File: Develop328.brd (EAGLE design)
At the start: 100 x 80 mm, 0 parts

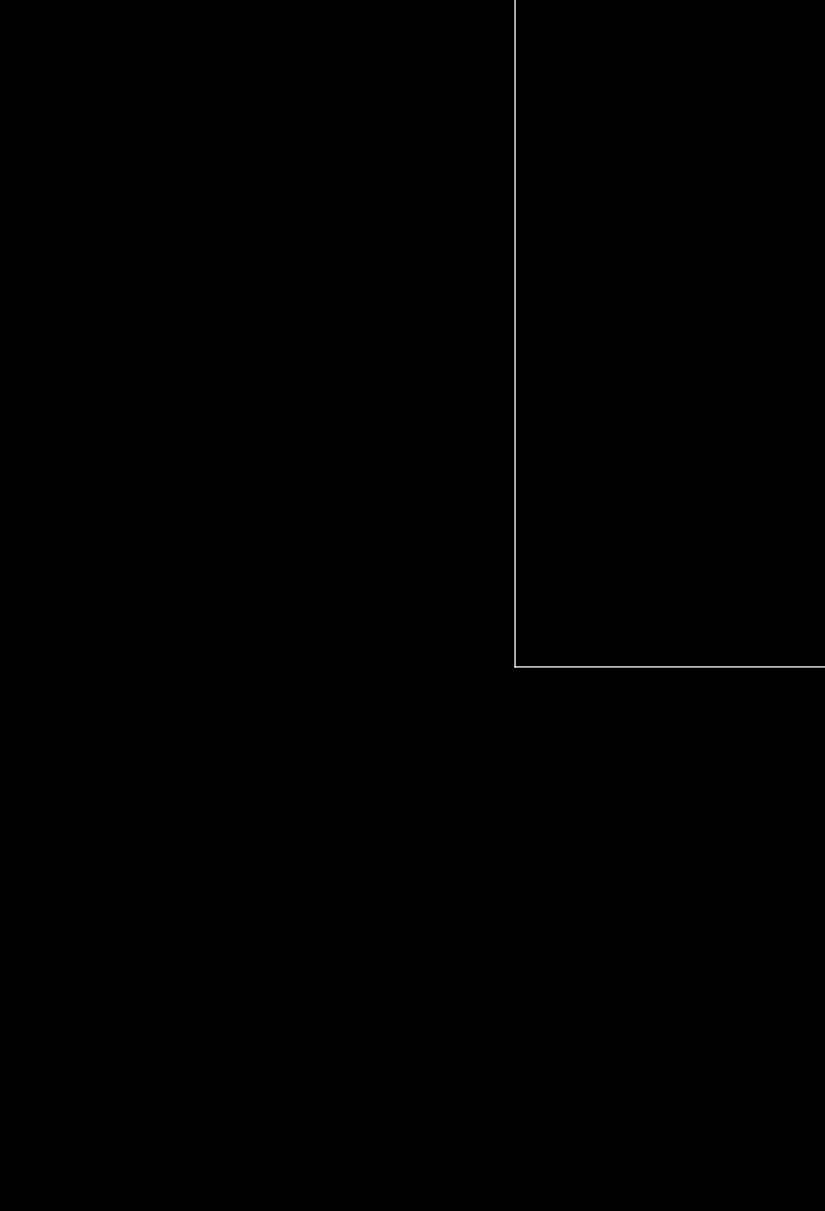
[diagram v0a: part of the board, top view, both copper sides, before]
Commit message: Added first round of components to schematic
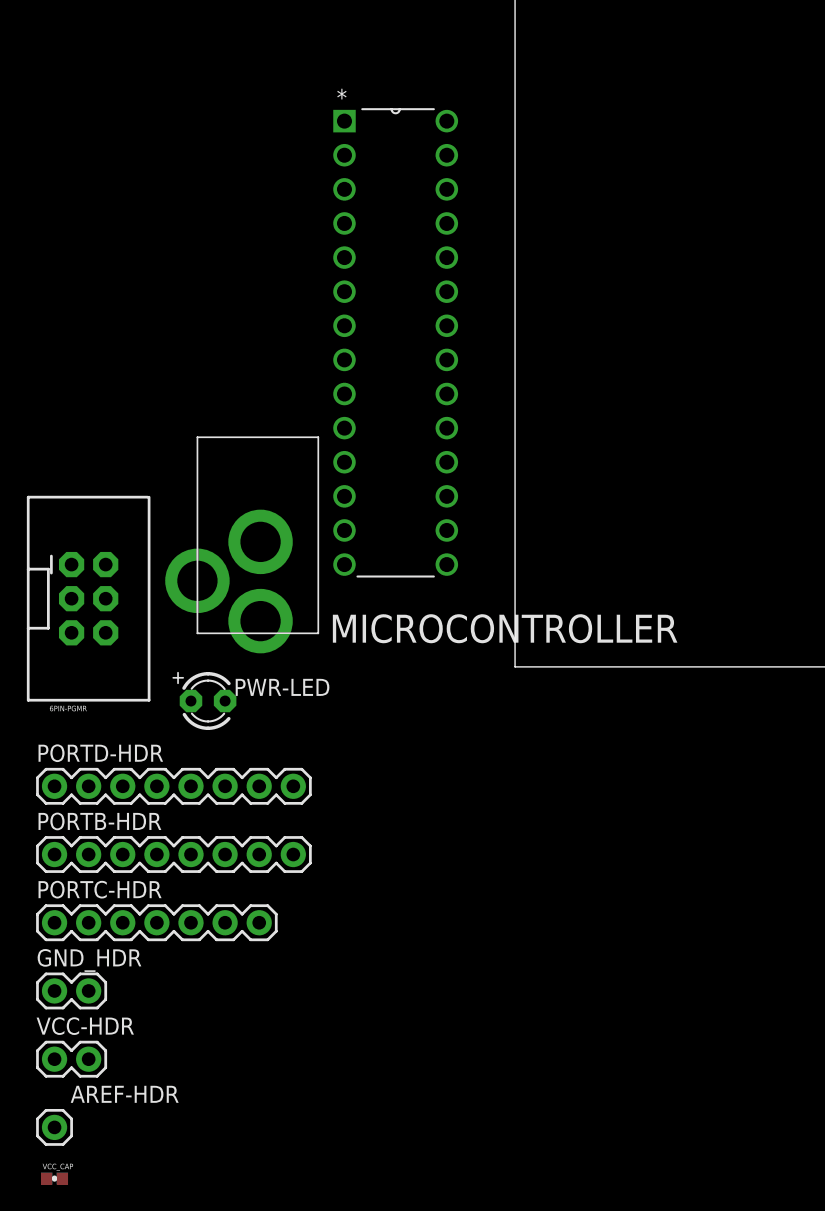
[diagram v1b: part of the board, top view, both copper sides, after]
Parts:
- added 5V-DC-JACK: (no value), adafruit:PJ-102A
- added 6PIN-PGMR: (no value), SparkFun-Connectors:2X3-SHROUDED
- added AREF-HDR: (no value), SparkFun-Connectors:1X01
- added GND_HDR, VCC-HDR: (no value), SparkFun-Connectors:1X02
- added MICROCONTROLLER: ATMEGA328P-PU, Atmel_By_element14_Batch_1-00:DIP254P762X457-28
- added PORTB-HDR, PORTD-HDR: (no value), SparkFun-Connectors:1X08_ROUND
- added PORTC-HDR: (no value), SparkFun-Connectors:1X07
- added PWR-LED: (no value), adafruit:LED3MM
- added VCC_CAP: 0.1uF, SparkFun-Capacitors:0402-CAP
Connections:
- new net AVCC: MICROCONTROLLER.20
- new net VCC: MICROCONTROLLER.7

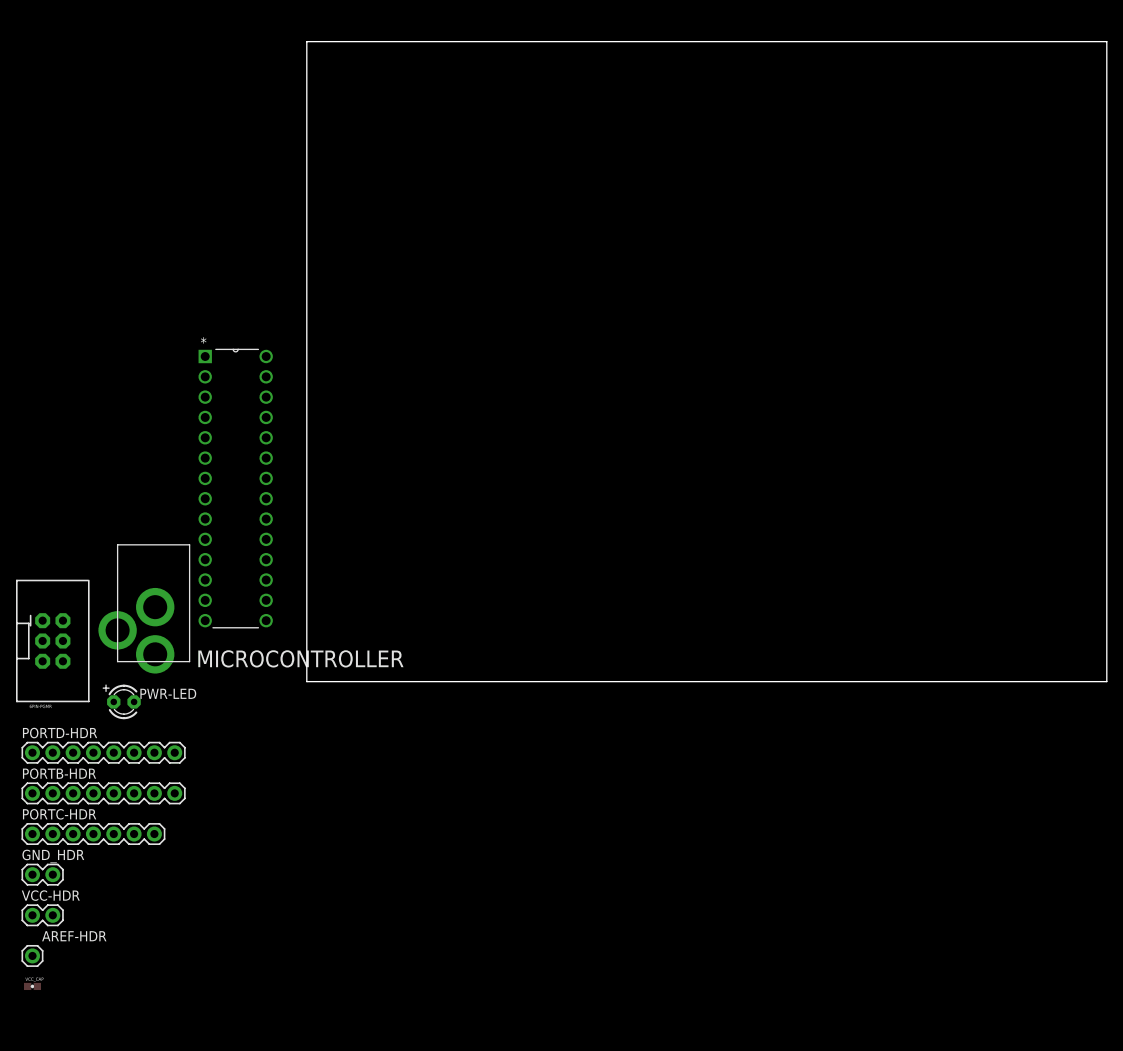
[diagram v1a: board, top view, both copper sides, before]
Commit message: Added wires to all port headers
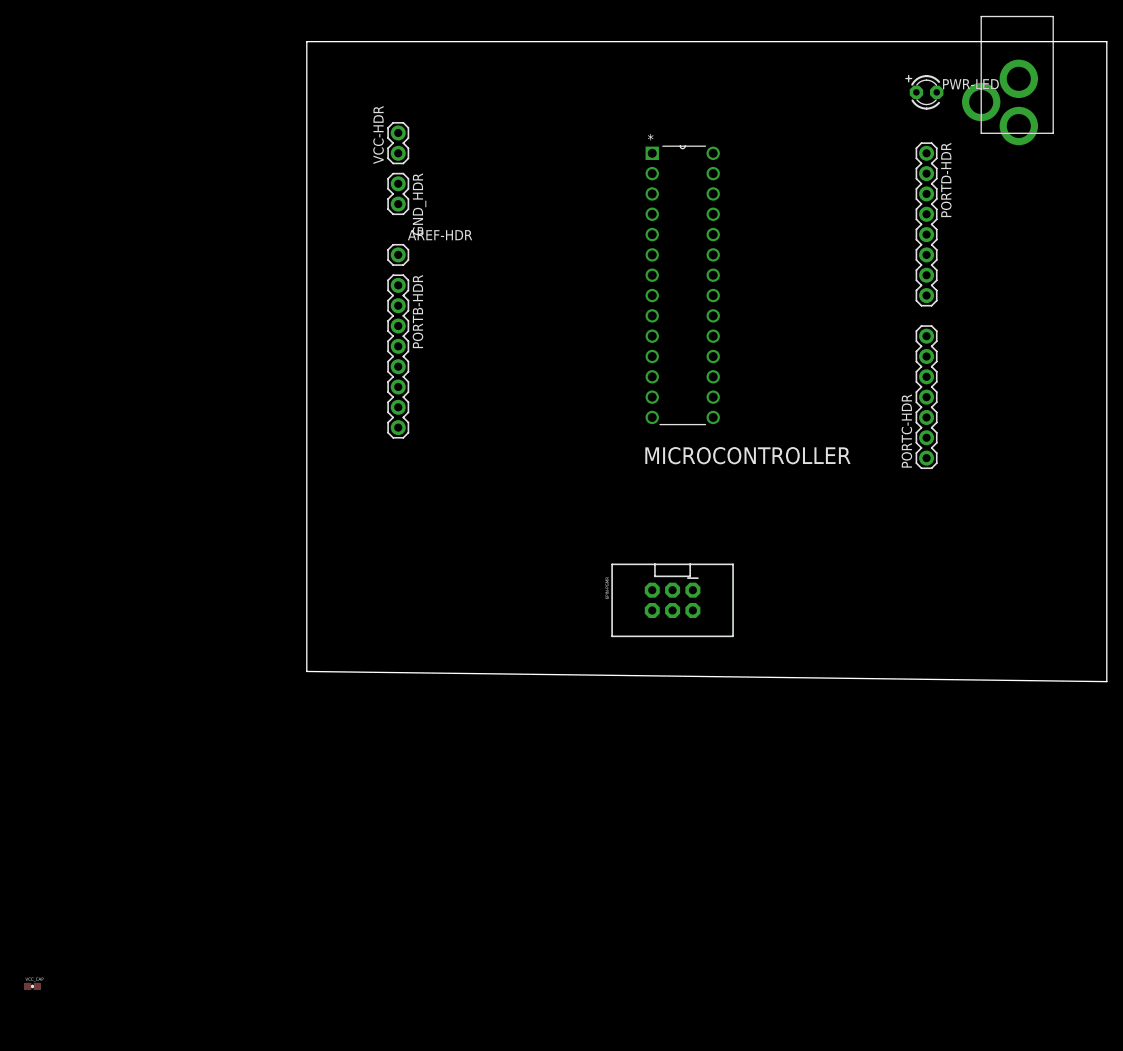
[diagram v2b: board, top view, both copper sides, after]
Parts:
- moved PORTD-HDR 134.6 mm to (77.5, 66.0), turned to 270 degrees
- moved 5V-DC-JACK 126.5 mm to (88.9, 78.7)
- moved PWR-LED 126.0 mm to (77.5, 73.7)
- moved PORTC-HDR 121.2 mm to (77.5, 27.9), turned to 90 degrees
- moved VCC-HDR 105.7 mm to (11.4, 66.0), turned to 90 degrees
- moved AREF-HDR 98.8 mm to (11.4, 53.3)
- moved GND_HDR 97.7 mm to (11.4, 62.2), turned to 270 degrees
- moved PORTB-HDR 78.2 mm to (11.4, 49.5), turned to 270 degrees
- moved 6PIN-PGMR 77.6 mm to (45.7, 10.2), turned to 270 degrees
- moved MICROCONTROLLER 61.4 mm to (50.8, 33.0)
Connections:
- removed net AVCC: MICROCONTROLLER.20
- removed net VCC: MICROCONTROLLER.7
- new net N$1: MICROCONTROLLER.7, VCC-HDR.2
- new net N$10: MICROCONTROLLER.13, PORTD-HDR.8
- new net N$11: MICROCONTROLLER.23, PORTC-HDR.1
- new net N$12: MICROCONTROLLER.24, PORTC-HDR.2
- new net N$13: MICROCONTROLLER.25, PORTC-HDR.3
- new net N$14: MICROCONTROLLER.26, PORTC-HDR.4
- new net N$15: MICROCONTROLLER.27, PORTC-HDR.5
- new net N$16: MICROCONTROLLER.28, PORTC-HDR.6
- new net N$17: MICROCONTROLLER.1, PORTC-HDR.7
- new net N$18: MICROCONTROLLER.14, PORTB-HDR.8
- new net N$19: MICROCONTROLLER.15, PORTB-HDR.7
- new net N$2: GND_HDR.1, MICROCONTROLLER.22
- new net N$20: MICROCONTROLLER.16, PORTB-HDR.6
- new net N$21: MICROCONTROLLER.17, PORTB-HDR.5
- new net N$22: MICROCONTROLLER.18, PORTB-HDR.4
- new net N$23: MICROCONTROLLER.19, PORTB-HDR.3
- new net N$24: MICROCONTROLLER.9, PORTB-HDR.2
- new net N$25: MICROCONTROLLER.10, PORTB-HDR.1
- new net N$26: AREF-HDR.1, MICROCONTROLLER.21
- new net N$27: MICROCONTROLLER.20, VCC-HDR.1
- new net N$28: GND_HDR.2, MICROCONTROLLER.8
- new net N$3: MICROCONTROLLER.2, PORTD-HDR.1
- new net N$4: MICROCONTROLLER.3, PORTD-HDR.2
- new net N$5: MICROCONTROLLER.4, PORTD-HDR.3
- new net N$6: MICROCONTROLLER.5, PORTD-HDR.4
- new net N$7: MICROCONTROLLER.6, PORTD-HDR.5
- new net N$8: MICROCONTROLLER.11, PORTD-HDR.6
- new net N$9: MICROCONTROLLER.12, PORTD-HDR.7
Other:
- outline, holes or cut-outs redrawn

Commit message: Replaced wires with electrical connections
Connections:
- removed net N$1 (its old number): MICROCONTROLLER.7, VCC-HDR.2
- removed net N$2 (its old number): GND_HDR.1, MICROCONTROLLER.22
- removed net N$27: MICROCONTROLLER.20, VCC-HDR.1
- removed net N$28: GND_HDR.2, MICROCONTROLLER.8
- new net AVCC: MICROCONTROLLER.20
- new net VCC: MICROCONTROLLER.7
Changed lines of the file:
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@@
 </elements>
 <signals>
-<signal name="N$2">
-<contactref element="MICROCONTROLLER" pad="22"/>
-<contactref element="GND_HDR" pad="1"/>
-<wire x1="11.43" y1="62.23" x2="50.8" y2="50.8" width="0" layer="19" extent="1-1"/>
+<signal name="VCC">
+<contactref element="MICROCONTROLLER" pad="7"/>
 </signal>
-<signal name="N$18">
+<signal name="AVCC">
+<contactref element="MICROCONTROLLER" pad="20"/>
+</signal>
+<signal name="N$1">
 <contactref element="PORTB-HDR" pad="8"/>
 <contactref element="MICROCONTROLLER" pad="14"/>
-<wire x1="43.18" y1="33.02" x2="11.43" y2="31.75" width="0" layer="19" extent="1-1"/>
+<wire x1="11.43" y1="31.75" x2="43.18" y2="33.02" width="0" layer="19" extent="1-1"/>
 </signal>
-<signal name="N$19">
+<signal name="N$2">
 <contactref element="PORTB-HDR" pad="7"/>
 <contactref element="MICROCONTROLLER" pad="15"/>
-<wire x1="50.8" y1="33.02" x2="11.43" y2="34.29" width="0" layer="19" extent="1-1"/>
+<wire x1="11.43" y1="34.29" x2="50.8" y2="33.02" width="0" layer="19" extent="1-1"/>
 </signal>
-<signal name="N$20">
+<signal name="N$3">
 <contactref element="PORTB-HDR" pad="6"/>
 <contactref element="MICROCONTROLLER" pad="16"/>
-<wire x1="50.8" y1="35.56" x2="11.43" y2="36.83" width="0" layer="19" extent="1-1"/>
+<wire x1="11.43" y1="36.83" x2="50.8" y2="35.56" width="0" layer="19" extent="1-1"/>
 </signal>
-<signal name="N$21">
+<signal name="N$4">
 <contactref element="PORTB-HDR" pad="5"/>
 <contactref element="MICROCONTROLLER" pad="17"/>
-<wire x1="50.8" y1="38.1" x2="11.43" y2="39.37" width="0" layer="19" extent="1-1"/>
+<wire x1="11.43" y1="39.37" x2="50.8" y2="38.1" width="0" layer="19" extent="1-1"/>
 </signal>
-<signal name="N$22">
+<signal name="N$5">
 <contactref element="PORTB-HDR" pad="4"/>
 <contactref element="MICROCONTROLLER" pad="18"/>
-<wire x1="50.8" y1="40.64" x2="11.43" y2="41.91" width="0" layer="19" extent="1-1"/>
+<wire x1="11.43" y1="41.91" x2="50.8" y2="40.64" width="0" layer="19" extent="1-1"/>
 </signal>
-<signal name="N$23">
+<signal name="N$6">
 <contactref element="PORTB-HDR" pad="3"/>
 <contactref element="MICROCONTROLLER" pad="19"/>
-<wire x1="50.8" y1="43.18" x2="11.43" y2="44.45" width="0" layer="19" extent="1-1"/>
+<wire x1="11.43" y1="44.45" x2="50.8" y2="43.18" width="0" layer="19" extent="1-1"/>
 </signal>
-<signal name="N$24">
+<signal name="N$7">
 <contactref element="PORTB-HDR" pad="2"/>
 <contactref element="MICROCONTROLLER" pad="9"/>
-<wire x1="43.18" y1="45.72" x2="11.43" y2="46.99" width="0" layer="19" extent="1-1"/>
+<wire x1="11.43" y1="46.99" x2="43.18" y2="45.72" width="0" layer="19" extent="1-1"/>
 </signal>
-<signal name="N$25">
+<signal name="N$8">
 <contactref element="PORTB-HDR" pad="1"/>
 <contactref element="MICROCONTROLLER" pad="10"/>
-<wire x1="43.18" y1="43.18" x2="11.43" y2="49.53" width="0" layer="19" extent="1-1"/>
+<wire x1="11.43" y1="49.53" x2="43.18" y2="43.18" width="0" layer="19" extent="1-1"/>
 </signal>
-<signal name="N$11">
+<signal name="N$9">
 <contactref element="PORTC-HDR" pad="1"/>
 <contactref element="MICROCONTROLLER" pad="23"/>
 <wire x1="50.8" y1="53.34" x2="77.47" y2="27.94" width="0" layer="19" extent="1-1"/>
 </signal>
-<signal name="N$12">
+<signal name="N$10">
 <contactref element="PORTC-HDR" pad="2"/>
 <contactref element="MICROCONTROLLER" pad="24"/>
 <wire x1="50.8" y1="55.88" x2="77.47" y2="30.48" width="0" layer="19" extent="1-1"/>
 </signal>
-<signal name="N$13">
+<signal name="N$11">
 <contactref element="PORTC-HDR" pad="3"/>
 <contactref element="MICROCONTROLLER" pad="25"/>
 <wire x1="50.8" y1="58.42" x2="77.47" y2="33.02" width="0" layer="19" extent="1-1"/>
 </signal>
-<signal name="N$15">
+<signal name="N$12">
+<contactref element="PORTC-HDR" pad="4"/>
+<contactref element="MICROCONTROLLER" pad="26"/>
+<wire x1="50.8" y1="60.96" x2="77.47" y2="35.56" width="0" layer="19" extent="1-1"/>
+</signal>
+<signal name="N$13">
 <contactref element="PORTC-HDR" pad="5"/>
 <contactref element="MICROCONTROLLER" pad="27"/>
 <wire x1="50.8" y1="63.5" x2="77.47" y2="38.1" width="0" layer="19" extent="1-1"/>
 </signal>
-<signal name="N$16">
+<signal name="N$14">
 <contactref element="PORTC-HDR" pad="6"/>
 <contactref element="MICROCONTROLLER" pad="28"/>
 <wire x1="50.8" y1="66.04" x2="77.47" y2="40.64" width="0" layer="19" extent="1-1"/>
 </signal>
-<signal name="N$17">
+<signal name="N$15">
 <contactref element="PORTC-HDR" pad="7"/>
 <contactref element="MICROCONTROLLER" pad="1"/>
 <wire x1="43.18" y1="66.04" x2="77.47" y2="43.18" width="0" layer="19" extent="1-1"/>
 </signal>
-<signal name="N$3">
+<signal name="N$16">
 <contactref element="PORTD-HDR" pad="1"/>
 <contactref element="MICROCONTROLLER" pad="2"/>
-<wire x1="77.47" y1="66.04" x2="43.18" y2="63.5" width="0" layer="19" extent="1-1"/>
+<wire x1="43.18" y1="63.5" x2="77.47" y2="66.04" width="0" layer="19" extent="1-1"/>
 </signal>
-<signal name="N$4">
+<signal name="N$17">
 <contactref element="PORTD-HDR" pad="2"/>
 <contactref element="MICROCONTROLLER" pad="3"/>
-<wire x1="77.47" y1="63.5" x2="43.18" y2="60.96" width="0" layer="19" extent="1-1"/>
+<wire x1="43.18" y1="60.96" x2="77.47" y2="63.5" width="0" layer="19" extent="1-1"/>
 </signal>
-<signal name="N$5">
+<signal name="N$18">
 <contactref element="PORTD-HDR" pad="3"/>
 <contactref element="MICROCONTROLLER" pad="4"/>
-<wire x1="77.47" y1="60.96" x2="43.18" y2="58.42" width="0" layer="19" extent="1-1"/>
+<wire x1="43.18" y1="58.42" x2="77.47" y2="60.96" width="0" layer="19" extent="1-1"/>
 </signal>
-<signal name="N$6">
+<signal name="N$19">
 <contactref element="PORTD-HDR" pad="4"/>
 <contactref element="MICROCONTROLLER" pad="5"/>
 <wire x1="43.18" y1="55.88" x2="77.47" y2="58.42" width="0" layer="19" extent="1-1"/>
 </signal>
-<signal name="N$7">
+<signal name="N$20">
 <contactref element="PORTD-HDR" pad="5"/>
 <contactref element="MICROCONTROLLER" pad="6"/>
 <wire x1="43.18" y1="53.34" x2="77.47" y2="55.88" width="0" layer="19" extent="1-1"/>
 </signal>
-<signal name="N$8">
+<signal name="N$21">
 <contactref element="PORTD-HDR" pad="6"/>
 <contactref element="MICROCONTROLLER" pad="11"/>
 <wire x1="43.18" y1="40.64" x2="77.47" y2="53.34" width="0" layer="19" extent="1-1"/>
 </signal>
-<signal name="N$9">
+<signal name="N$22">
 <contactref element="PORTD-HDR" pad="7"/>
 <contactref element="MICROCONTROLLER" pad="12"/>
 <wire x1="43.18" y1="38.1" x2="77.47" y2="50.8" width="0" layer="19" extent="1-1"/>
 </signal>
-<signal name="N$10">
+<signal name="N$23">
 <contactref element="PORTD-HDR" pad="8"/>
 <contactref element="MICROCONTROLLER" pad="13"/>
 <wire x1="43.18" y1="35.56" x2="77.47" y2="48.26" width="0" layer="19" extent="1-1"/>
 </signal>
-<signal name="N$26">
+<signal name="N$24">
 <contactref element="AREF-HDR" pad="1"/>
 <contactref element="MICROCONTROLLER" pad="21"/>
-<wire x1="50.8" y1="48.26" x2="11.43" y2="53.34" width="0" layer="19" extent="1-1"/>
-</signal>
-<signal name="N$1">
-<contactref element="MICROCONTROLLER" pad="7"/>
-<contactref element="VCC-HDR" pad="2"/>
-<wire x1="11.43" y1="68.58" x2="43.18" y2="50.8" width="0" layer="19" extent="1-1"/>
-</signal>
-<signal name="N$27">
-<contactref element="MICROCONTROLLER" pad="20"/>
-<contactref element="VCC-HDR" pad="1"/>
-<wire x1="50.8" y1="45.72" x2="11.43" y2="66.04" width="0" layer="19" extent="1-1"/>
-</signal>
-<signal name="N$28">
-<contactref element="MICROCONTROLLER" pad="8"/>
-<contactref element="GND_HDR" pad="2"/>
-<wire x1="43.18" y1="48.26" x2="11.43" y2="59.69" width="0" layer="19" extent="1-1"/>
-</signal>
-<signal name="N$14">
-<contactref element="PORTC-HDR" pad="4"/>
-<contactref element="MICROCONTROLLER" pad="26"/>
-<wire x1="50.8" y1="60.96" x2="77.47" y2="35.56" width="0" layer="19" extent="1-1"/>
+<wire x1="11.43" y1="53.34" x2="50.8" y2="48.26" width="0" layer="19" extent="1-1"/>
 </signal>
 </signals>
